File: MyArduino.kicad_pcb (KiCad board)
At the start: 2 copper layers, 56 x 69.3 mm, 32 parts, among them J1 PWR, J10 , J11 , J2 ISP, J3 VCC, J4 GND, J5 IOH, J6 AD, J7 IOL, J8 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

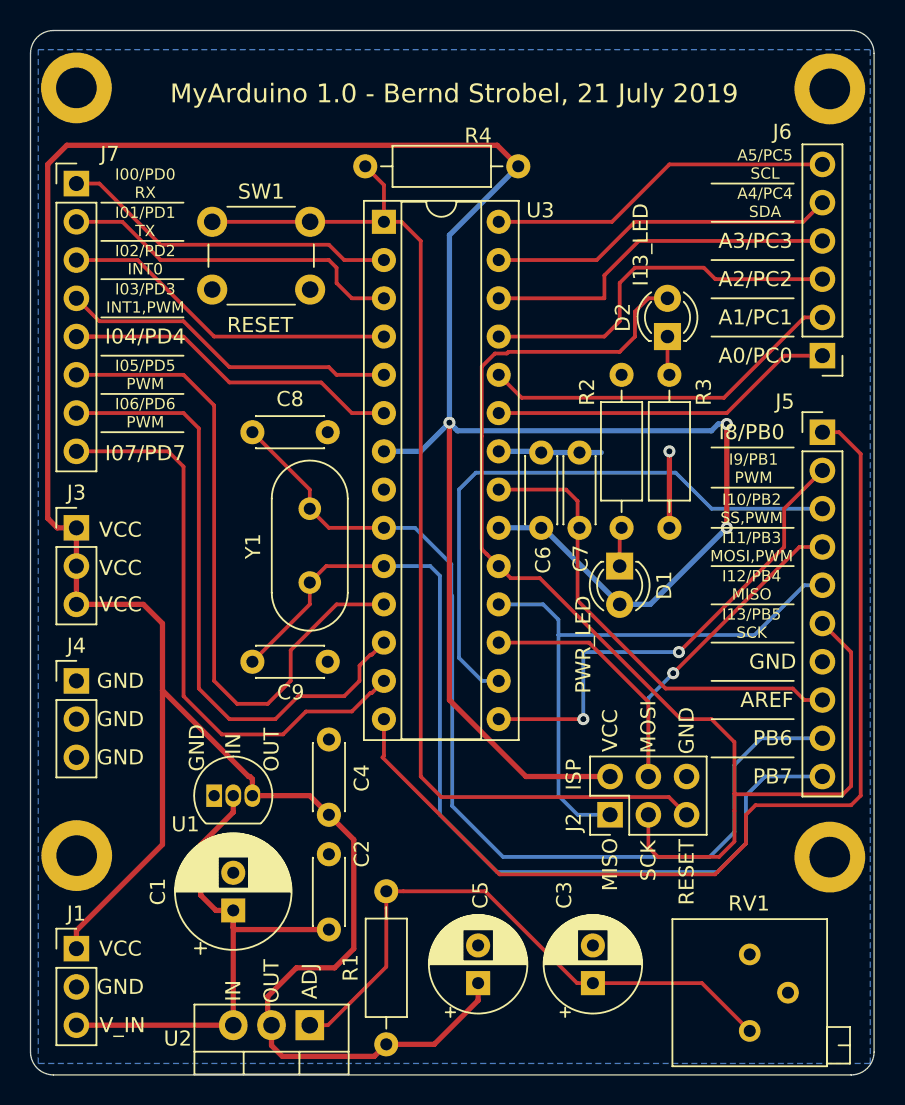
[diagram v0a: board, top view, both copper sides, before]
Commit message: Improved routing and power traces width
Version 1.1
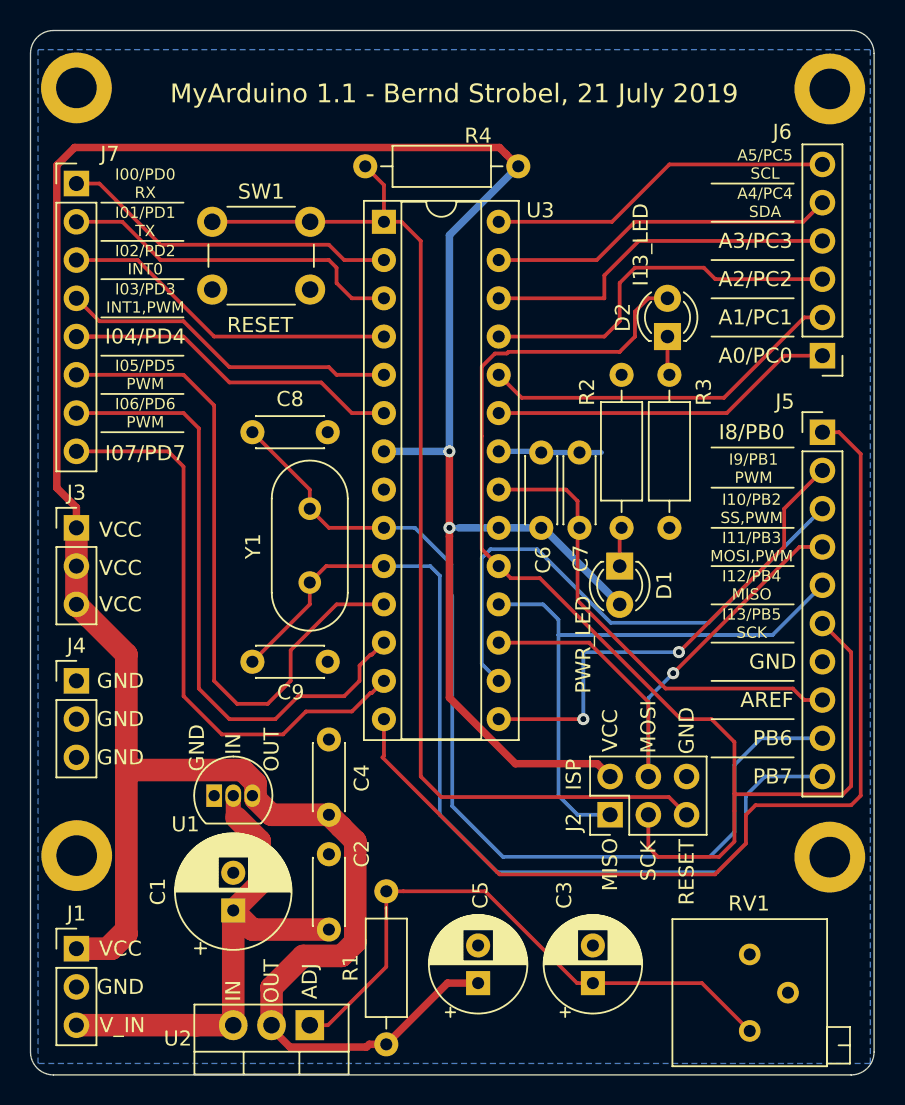
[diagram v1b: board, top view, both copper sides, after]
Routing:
- net /V_UNREG: track 35.7 -> 55.1 mm
- net GND: track 11.9 -> 6.84 mm, vias 1 -> 0
- net /SS: track 40.0 -> 36.6 mm
- net VCC: track 245.6 -> 247.2 mm, vias 3 -> 2
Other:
- net class Power: trace_width 0.35 -> 0.5; via_dia 0.8 -> 1.6; via_drill 0.4 -> 0.8
- board text added: "MyArduino 1.1 - Bernd Strobel, 21 July 2019"
- board text removed: "MyArduino 1.0 - Bernd Strobel, 21 July 2019"
